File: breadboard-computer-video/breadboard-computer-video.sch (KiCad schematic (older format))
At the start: 20 parts, among them Q1 Q_NPN_BCE, Q2 Q_NPN_BCE, U1 74LS04, U2 74LS163, U3 74LS32, U4 74LS08, U5 74LS163, U6 74LS14, U7 28C256, U8 74LS02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

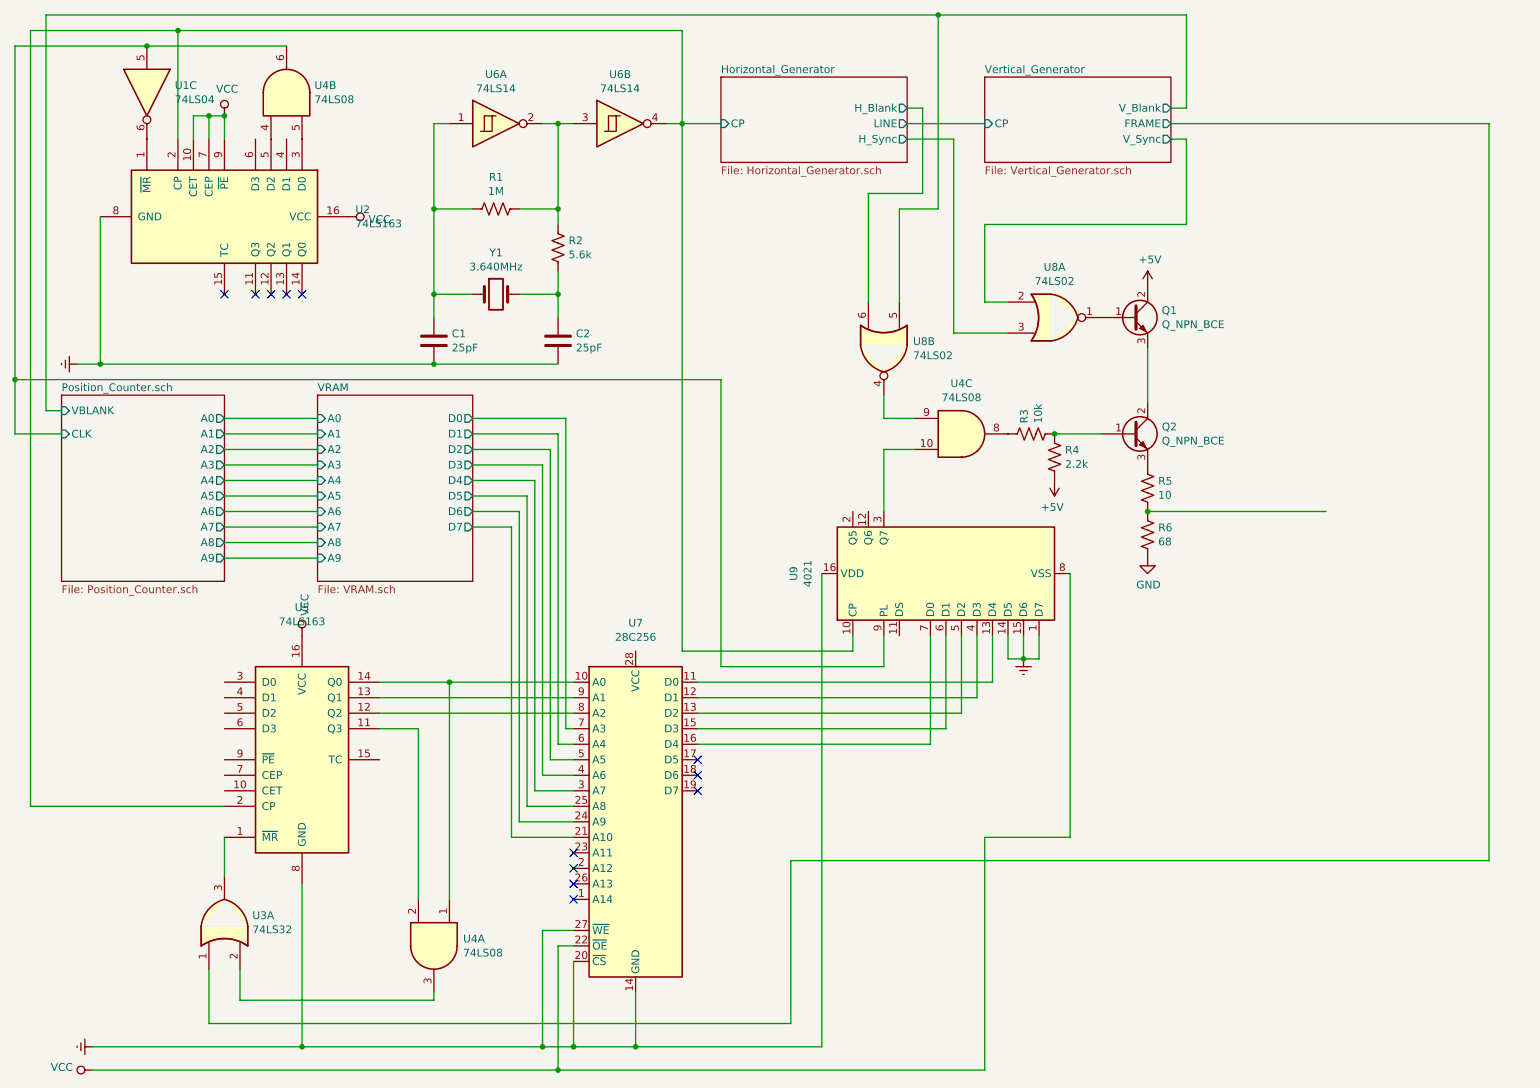
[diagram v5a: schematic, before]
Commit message: Eliminated a redundant 74ls163, which was only necessary when the character cells were not of equal width and height
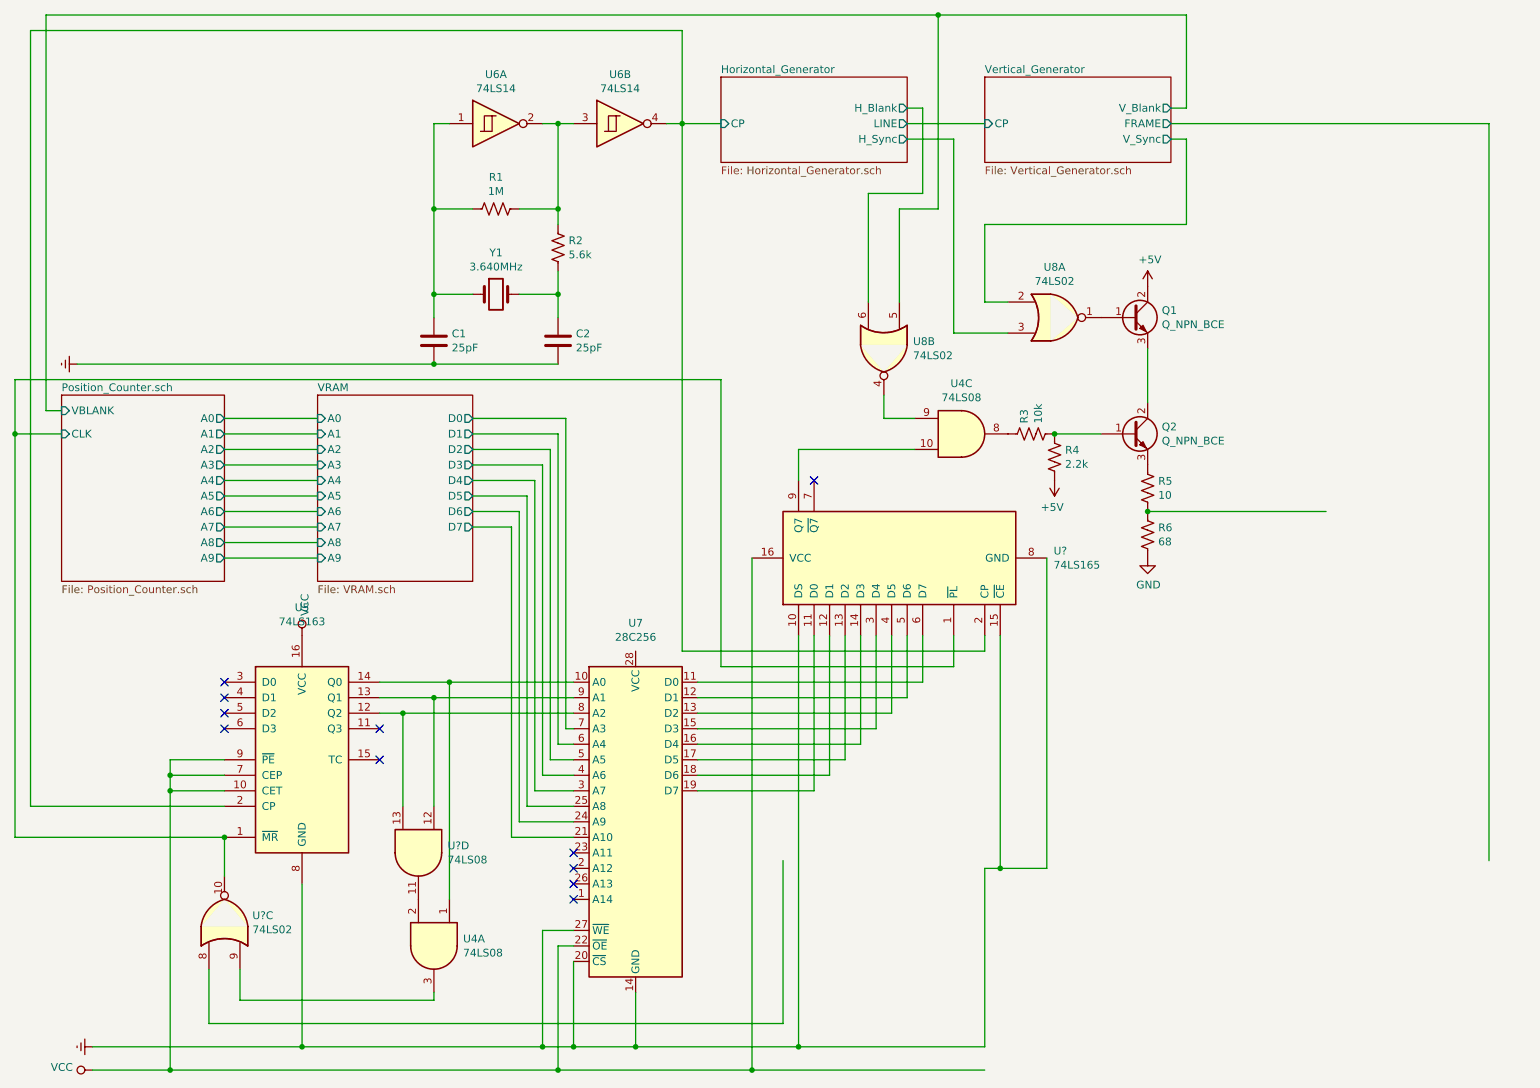
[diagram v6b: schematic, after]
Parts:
- removed U1: 74LS04, symbol 74xx:74LS04
- removed U2: 74LS163, symbol 74xx:74LS163
- removed U3: 74LS32, symbol 74xx:74LS32
- removed unit 2 of U4
- removed U9: 4021, symbol 4xxx:4021
- added U?: 74LS02, symbol 74xx:74LS02
- added U?: 74LS08, symbol 74xx:74LS08
- added U?: 74LS165, symbol 74xx:74LS165
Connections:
- net Earth: now also U?.10 (DS), U?.15 (~CE), U?.8 (GND)
- net Horizontal_Generator/CP: now also U?.2 (CP)
- net Position_Counter.sch/CLK: now also U5.1 (~MR), U?.1 (~PL), U?.10
- net VCC: now also U5.10 (CET), U5.7 (CEP), U5.9 (~PE), U?.16 (VCC)
- net at U7.11 (D0): now also U?.6 (D7)
- net at U4.10: now also U?.9 (Q7)
- net at U7.12 (D1): now also U?.5 (D6)
- net at U7.13 (D2): now also U?.4 (D5)
- net at U7.15 (D3): now also U?.3 (D4)
- net at U7.16 (D4): now also U?.14 (D3)
- net at U4.2: now also U?.11; no longer U5.11 (Q3)
- net at U4.3: now also U?.9
- net at U5.12 (Q2), U7.8 (A2): now also U?.13
- net at U5.13 (Q1), U7.9 (A1): now also U?.12
- net at U7.17 (D5): now also U?.13 (D2)
- net at U7.18 (D6): now also U?.12 (D1)
- net at U7.19 (D7): now also U?.11 (D0)
- no-connect marks 12 -> 11
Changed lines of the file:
@@
 $EndComp
-Wire Wire Line
-	5000 5200 6900 5200
-Wire Wire Line
-	5000 5300 6800 5300
-Wire Wire Line
-	5000 5400 6700 5400
-Wire Wire Line
-	5000 5500 6600 5500
 Wire Wire Line
 	4200 5200 3400 5200
@@
 $EndComp
 Wire Wire Line
-	2950 5500 3200 5500
-Wire Wire Line
-	3200 5500 3200 6600
-Wire Wire Line
 	8050 1600 10100 1600
 Wire Wire Line
 	10100 1600 10100 6350
 Wire Wire Line
-	10100 6350 5600 6350
-Wire Wire Line
-	5600 6350 5600 7400
-Wire Wire Line
-	5600 7400 1850 7400
+	5550 6350 5550 7400
+Wire Wire Line
+	5550 7400 1850 7400
 Wire Wire Line
 	1850 7400 1850 7050
@@
 Wire Wire Line
 	1950 6200 1950 6450
-$Comp
-L 74xx:74LS32 U3
-U 1 1 5DC0297B
-P 1950 6750
-F 0 "U3" V 1996 6570 50  0000 R CNN
-F 1 "74LS32" V 1905 6570 50  0000 R CNN
-F 2 "" H 1950 6750 50  0001 C CNN
-F 3 "http://www.ti.com/lit/gpn/sn74LS32" H 1950 6750 50  0001 C CNN
-	1    1950 6750
-	0    -1   -1   0
-$EndComp
 Wire Wire Line
 	2050 7050 2050 7250
@@
 Wire Wire Line
 	4900 1600 4900 1000
-Wire Wire Line
-	4900 1000 1650 1000
 Wire Wire Line
 	700  1000 700  6000
@@
 	3400 6600 3400 5400
 Wire Wire Line
-	6000 5000 4900 5000
-Wire Wire Line
 	4900 5000 4900 1600
 Wire Wire Line
-	2950 5400 4200 5400
-Wire Wire Line
-	2950 5300 3400 5300
+	2950 5400 3100 5400
+Wire Wire Line
+	2950 5300 3300 5300
 Connection ~ 3400 5200
 Wire Wire Line
@@
 $EndComp
 Wire Wire Line
-	5000 5600 6500 5600
-NoConn ~ 5000 5900
-NoConn ~ 5000 5800
-NoConn ~ 5000 5700
-Wire Wire Line
 	3550 3500 4150 3500
 Wire Wire Line
@@
 Connection ~ 2450 7550
 Wire Wire Line
-	2450 7550 1100 7550
-Wire Wire Line
-	6500 4900 6500 5600
-Wire Wire Line
-	6600 4900 6600 5500
-Wire Wire Line
-	6700 4900 6700 5400
-Wire Wire Line
-	6800 4900 6800 5300
-Wire Wire Line
-	6900 5200 6900 4900
-Wire Wire Line
-	6000 4900 6000 5000
-Wire Wire Line
-	4600 7550 5800 7550
-$Comp
-L 4xxx:4021 U9
-U 1 1 5D92BCAE
-P 6600 4500
-F 0 "U9" H 6600 5481 50  0000 C CNN
-F 1 "4021" H 6600 5390 50  0000 C CNN
-F 2 "" H 6600 4650 50  0001 C CNN
-F 3 "https://assets.nexperia.com/documents/data-sheet/HEF4021B.pdf" H 6600 4650 50  0001 C CNN
-	1    6600 4500
-	0    -1   -1   0
-$EndComp
-Wire Wire Line
-	5800 4500 5800 7550
-Wire Wire Line
 	4200 6900 4100 6900
 Wire Wire Line
@@
 	4000 7550 4200 7550
 Wire Wire Line
-	6850 7700 4100 7700
-Wire Wire Line
-	6850 7700 6850 6200
-Wire Wire Line
-	6850 6200 7400 6200
-Wire Wire Line
-	7400 6200 7400 4500
+	6850 7700 5350 7700
 Wire Wire Line
 	4100 6900 4100 7700
 Connection ~ 4100 7700
 Wire Wire Line
-	4100 7700 1100 7700
+	4100 7700 1600 7700
 $Comp
 L power:VCC #PWR?
@@
 Wire Wire Line
 	800  3450 900  3450
-$Comp
-L 74xx:74LS163 U2
-U 1 1 5E36C15A
-P 1950 2200
-F 0 "U2" V 1904 3044 50  0000 L CNN
-F 1 "74LS163" V 1995 3044 50  0000 L CNN
-F 2 "" H 1950 2200 50  0001 C CNN
-F 3 "http://www.ti.com/lit/gpn/sn74LS163" H 1950 2200 50  0001 C CNN
-	1    1950 2200
-	0    1    1    0
-$EndComp
-Wire Wire Line
-	1650 1700 1650 1000
-Connection ~ 1650 1000
-Wire Wire Line
-	1650 1000 700  1000
-$Comp
-L 74xx:74LS08 U4
-U 2 1 5E37DDE5
-P 2350 1400
-F 0 "U4" V 2396 1220 50  0000 R CNN
-F 1 "74LS08" V 2305 1220 50  0000 R CNN
-F 2 "" H 2350 1400 50  0001 C CNN
-F 3 "http://www.ti.com/lit/gpn/sn74LS08" H 2350 1400 50  0001 C CNN
-	2    2350 1400
-	0    -1   -1   0
-$EndComp
-Wire Wire Line
-	2350 1100 1450 1100
-Wire Wire Line
-	1450 1100 600  1100
 Wire Wire Line
 	600  3600 900  3600
-Connection ~ 1450 1100
-NoConn ~ 2450 2700
-NoConn ~ 2350 2700
-NoConn ~ 2250 2700
-NoConn ~ 2150 2700
-NoConn ~ 1950 2700
-$Comp
-L 74xx:74LS04 U1
-U 3 1 5E3AF993
-P 1450 1400
-F 0 "U1" V 1404 1580 50  0000 L CNN
-F 1 "74LS04" V 1495 1580 50  0000 L CNN
-F 2 "" H 1450 1400 50  0001 C CNN
-F 3 "http://www.ti.com/lit/gpn/sn74LS04" H 1450 1400 50  0001 C CNN
-	3    1450 1400
-	0    1    1    0
-$EndComp
-$Comp
-L power:VCC #PWR?
-U 1 1 5E3BFB68
-P 1950 1550
-F 0 "#PWR?" H 1950 1400 50  0001 C CNN
-F 1 "VCC" H 1967 1723 50  0000 C CNN
-F 2 "" H 1950 1550 50  0001 C CNN
-F 3 "" H 1950 1550 50  0001 C CNN
-	1    1950 1550
-	1    0    0    -1
-$EndComp
-Wire Wire Line
-	1950 1550 1850 1550
-Wire Wire Line
-	1750 1550 1750 1700
-Wire Wire Line
-	1850 1700 1850 1550
-Connection ~ 1850 1550
-Wire Wire Line
-	1850 1550 1750 1550
-Wire Wire Line
-	1950 1550 1950 1700
-Connection ~ 1950 1550
-$Comp
-L power:Earth #PWR?
-U 1 1 5E3D9597
-P 7100 5050
-F 0 "#PWR?" H 7100 4800 50  0001 C CNN
-F 1 "Earth" H 7100 4900 50  0001 C CNN
-F 2 "" H 7100 5050 50  0001 C CNN
-F 3 "~" H 7100 5050 50  0001 C CNN
-	1    7100 5050
-	1    0    0    -1
-$EndComp
-Wire Wire Line
-	7100 5050 7100 4900
-Wire Wire Line
-	7000 4900 7000 5050
-Wire Wire Line
-	7000 5050 7100 5050
-Connection ~ 7100 5050
-Wire Wire Line
-	7100 5050 7200 5050
-Wire Wire Line
-	7200 5050 7200 4900
-Wire Wire Line
-	6200 4900 6200 5100
-Wire Wire Line
-	6200 5100 5150 5100
+Wire Wire Line
+	6650 5100 5150 5100
 Wire Wire Line
 	3550 4200 3800 4200
@@
 	5150 3250 5150 5100
 Wire Wire Line
-	600  1100 600  3250
-Wire Wire Line
 	600  3250 600  3600
-Connection ~ 600  3250
 Wire Wire Line
 	1950 3500 2550 3500
@@
 	4100 3150 3300 3150
 Connection ~ 3300 3150
-Wire Wire Line
-	3300 3150 1150 3150
-Connection ~ 1150 3150
-Wire Wire Line
-	1150 3150 1000 3150
-Wire Wire Line
-	1150 2200 1150 3150
 $Comp
 L power:Earth #PWR?
@@
 $EndComp
 $Comp
-L power:VCC #PWR?
-U 1 1 5E98E66C
-P 2750 2200
-F 0 "#PWR?" H 2750 2050 50  0001 C CNN
-F 1 "VCC" V 2767 2328 50  0000 L CNN
-F 2 "" H 2750 2200 50  0001 C CNN
-F 3 "" H 2750 2200 50  0001 C CNN
-	1    2750 2200
-	0    1    1    0
-$EndComp
-$Comp
 L 74xx:74LS08 U4
 U 3 1 5E99B421
@@
 $EndComp
 Wire Wire Line
-	6400 3700 6200 3700
-Wire Wire Line
-	6200 3700 6200 4100
-Wire Wire Line
 	6200 3350 6200 3500
 Wire Wire Line
@@
 	1    0    0    -1
 $EndComp
+$Comp
+L 74xx:74LS02 U?
+U 3 1 5DC8E486
+P 1950 6750
+F 0 "U?" V 1996 6570 50  0000 R CNN
+F 1 "74LS02" V 1905 6570 50  0000 R CNN
+F 2 "" H 1950 6750 50  0001 C CNN
+F 3 "http://www.ti.com/lit/gpn/sn74ls02" H 1950 6750 50  0001 C CNN
+	3    1950 6750
+	0    -1   -1   0
+$EndComp
+NoConn ~ 1950 5500
+NoConn ~ 1950 5400
+NoConn ~ 1950 5300
+NoConn ~ 1950 5200
+Wire Wire Line
+	1950 5700 1600 5700
+Wire Wire Line
+	1600 5700 1600 5800
+Connection ~ 1600 7700
+Wire Wire Line
+	1600 7700 1100 7700
+NoConn ~ 2950 5700
+$Comp
+L 74xx:74LS08 U?
+U 4 1 5DCE6604
+P 3200 6300
+F 0 "U?" V 3154 6488 50  0000 L CNN
+F 1 "74LS08" V 3245 6488 50  0000 L CNN
+F 2 "" H 3200 6300 50  0001 C CNN
+F 3 "http://www.ti.com/lit/gpn/sn74LS08" H 3200 6300 50  0001 C CNN
+	4    3200 6300
+	0    1    1    0
+$EndComp
+Wire Wire Line
+	3100 6000 3100 5400
+Connection ~ 3100 5400
+Wire Wire Line
+	3100 5400 4200 5400
+Wire Wire Line
+	3300 6000 3300 5300
+Connection ~ 3300 5300
+Wire Wire Line
+	3300 5300 3400 5300
+Wire Wire Line
+	5000 5400 6250 5400
+Wire Wire Line
+	5000 5500 6150 5500
+Wire Wire Line
+	5000 5600 6050 5600
+Wire Wire Line
+	5000 5700 5950 5700
+Wire Wire Line
+	5000 5800 5850 5800
+Wire Wire Line
+	5000 5900 5750 5900
+$Comp
+L 74xx:74LS165 U?
+U 1 1 5DD7AB27
+P 6250 4400
+F 0 "U?" V 6296 3356 50  0000 R CNN
+F 1 "74LS165" V 6205 3356 50  0000 R CNN
+F 2 "" H 6250 4400 50  0001 C CNN
+F 3 "http://www.ti.com/lit/gpn/sn74LS165" H 6250 4400 50  0001 C CNN
+	1    6250 4400
+	0    -1   -1   0
+$EndComp
+Wire Wire Line
+	5000 5200 6450 5200
+Wire Wire Line
+	5000 5300 6350 5300
+Wire Wire Line
+	6650 4900 6650 5100
+Wire Wire Line
+	5750 5900 5750 4900
+Wire Wire Line
+	5850 5800 5850 4900
+Wire Wire Line
+	5950 5700 5950 4900
+Wire Wire Line
+	6350 4900 6350 5300
+Wire Wire Line
+	6250 4900 6250 5400
+Wire Wire Line
+	6850 4900 6850 5000
+Wire Wire Line
+	6450 5200 6450 4900
+Wire Wire Line
+	6050 4900 6050 5600
+Wire Wire Line
+	6150 4900 6150 5500
+Wire Wire Line
+	6850 5000 4900 5000
+Wire Wire Line
+	5650 3700 5650 3900
+Wire Wire Line
+	5650 3700 6400 3700
+Wire Wire Line
+	6850 7550 6850 6400
+Wire Wire Line
+	4600 7550 5650 7550
+Wire Wire Line
+	5350 7700 5350 4400
+Connection ~ 5350 7700
+Wire Wire Line
+	5350 7700 4100 7700
+Wire Wire Line
+	7250 4400 7250 6400
+Wire Wire Line
+	6850 6400 6950 6400
+Wire Wire Line
+	5650 4900 5650 7550
+Connection ~ 5650 7550
+Wire Wire Line
+	5650 7550 6850 7550
+Wire Wire Line
+	6950 4900 6950 6400
+Connection ~ 6950 6400
+Wire Wire Line
+	6950 6400 7250 6400
+NoConn ~ 5750 3900
+Wire Wire Line
+	1100 7550 2450 7550
+Wire Wire Line
+	1600 5800 1950 5800
+Connection ~ 1600 5800
+Wire Wire Line
+	1600 5800 1600 5900
+Wire Wire Line
+	1600 5900 1950 5900
+Connection ~ 1600 5900
+Wire Wire Line
+	1600 5900 1600 7700
+Wire Wire Line
+	700  1000 4900 1000
+Wire Wire Line
+	1000 3150 3300 3150
+Wire Wire Line
+	600  3600 600  6200
+Wire Wire Line
+	600  6200 1950 6200
+Connection ~ 600  3600
+Connection ~ 1950 6200
+NoConn ~ 2950 5500
 $EndSCHEMATC

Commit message: various things
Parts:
- Y1: value 3.640MHz -> 12MHz
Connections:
- net Vertical_Generator/FRAME: now also U?.8
- net CVBS_Output: now reaches R5.2, R6.1
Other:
- moved on the sheet: C1, C2, R1, R2, U6A, U6B, Y1
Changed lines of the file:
@@
 L Device:C C1
 U 1 1 5D9AD126
-P 3300 3000
-F 0 "C1" H 3415 3046 50  0000 L CNN
-F 1 "25pF" H 3415 2955 50  0000 L CNN
-F 2 "" H 3338 2850 50  0001 C CNN
-F 3 "~" H 3300 3000 50  0001 C CNN
-	1    3300 3000
+P 3200 3000
+F 0 "C1" H 3315 3046 50  0000 L CNN
+F 1 "25pF" H 3315 2955 50  0000 L CNN
+F 2 "" H 3238 2850 50  0001 C CNN
+F 3 "~" H 3200 3000 50  0001 C CNN
+	1    3200 3000
 	1    0    0    -1
 $EndComp
@@
 L Device:C C2
 U 1 1 5D9ADB4B
-P 4100 3000
-F 0 "C2" H 4215 3046 50  0000 L CNN
-F 1 "25pF" H 4215 2955 50  0000 L CNN
-F 2 "" H 4138 2850 50  0001 C CNN
-F 3 "~" H 4100 3000 50  0001 C CNN
-	1    4100 3000
+P 4000 3000
+F 0 "C2" H 4115 3046 50  0000 L CNN
+F 1 "25pF" H 4115 2955 50  0000 L CNN
+F 2 "" H 4038 2850 50  0001 C CNN
+F 3 "~" H 4000 3000 50  0001 C CNN
+	1    4000 3000
 	1    0    0    -1
 $EndComp
@@
 L Device:Crystal Y1
 U 1 1 5D9AE745
-P 3700 2700
-F 0 "Y1" H 3700 2968 50  0000 C CNN
-F 1 "3.640MHz" H 3700 2877 50  0000 C CNN
-F 2 "" H 3700 2700 50  0001 C CNN
-F 3 "https://www.mouser.com/datasheet/2/741/LFXTAL036736Bulk-998720.pdf" H 3700 2700 50  0001 C CNN
-	1    3700 2700
+P 3600 2700
+F 0 "Y1" H 3600 2968 50  0000 C CNN
+F 1 "12MHz" H 3600 2877 50  0000 C CNN
+F 2 "" H 3600 2700 50  0001 C CNN
+F 3 "https://www.mouser.com/datasheet/2/741/LFXTAL036736Bulk-998720.pdf" H 3600 2700 50  0001 C CNN
+	1    3600 2700
 	1    0    0    -1
 $EndComp
@@
 L Device:R_US R2
 U 1 1 5D9AF295
-P 4100 2400
-F 0 "R2" H 4168 2446 50  0000 L CNN
-F 1 "5.6k" H 4168 2355 50  0000 L CNN
-F 2 "" V 4140 2390 50  0001 C CNN
-F 3 "~" H 4100 2400 50  0001 C CNN
-	1    4100 2400
+P 4000 2400
+F 0 "R2" H 4068 2446 50  0000 L CNN
+F 1 "5.6k" H 4068 2355 50  0000 L CNN
+F 2 "" V 4040 2390 50  0001 C CNN
+F 3 "~" H 4000 2400 50  0001 C CNN
+	1    4000 2400
 	1    0    0    -1
 $EndComp
@@
 L Device:R_US R1
 U 1 1 5D9AFC84
-P 3700 2150
-F 0 "R1" V 3495 2150 50  0000 C CNN
-F 1 "1M" V 3586 2150 50  0000 C CNN
-F 2 "" V 3740 2140 50  0001 C CNN
-F 3 "~" H 3700 2150 50  0001 C CNN
-	1    3700 2150
+P 3600 2150
+F 0 "R1" V 3395 2150 50  0000 C CNN
+F 1 "1M" V 3486 2150 50  0000 C CNN
+F 2 "" V 3640 2140 50  0001 C CNN
+F 3 "~" H 3600 2150 50  0001 C CNN
+	1    3600 2150
 	0    1    1    0
 $EndComp
 Wire Wire Line
-	3300 2850 3300 2700
-Wire Wire Line
-	3300 1600 3400 1600
-Wire Wire Line
-	4000 1600 4100 1600
-Wire Wire Line
-	4100 1600 4100 2150
-Wire Wire Line
-	4100 2550 4100 2700
-Wire Wire Line
-	3850 2700 4100 2700
-Connection ~ 4100 2700
-Wire Wire Line
-	4100 2700 4100 2850
-Wire Wire Line
-	3550 2700 3300 2700
-Connection ~ 3300 2700
-Wire Wire Line
-	3300 2700 3300 2150
-Wire Wire Line
-	3550 2150 3300 2150
-Connection ~ 3300 2150
-Wire Wire Line
-	3300 2150 3300 1600
-Wire Wire Line
-	3850 2150 4100 2150
-Connection ~ 4100 2150
-Wire Wire Line
-	4100 2150 4100 2250
-Wire Wire Line
-	4200 1600 4100 1600
-Connection ~ 4100 1600
+	3200 2850 3200 2700
+Wire Wire Line
+	3200 1600 3300 1600
+Wire Wire Line
+	3900 1600 4000 1600
+Wire Wire Line
+	4000 1600 4000 2150
+Wire Wire Line
+	4000 2550 4000 2700
+Wire Wire Line
+	3750 2700 4000 2700
+Connection ~ 4000 2700
+Wire Wire Line
+	4000 2700 4000 2850
+Wire Wire Line
+	3450 2700 3200 2700
+Connection ~ 3200 2700
+Wire Wire Line
+	3200 2700 3200 2150
+Wire Wire Line
+	3450 2150 3200 2150
+Connection ~ 3200 2150
+Wire Wire Line
+	3200 2150 3200 1600
+Wire Wire Line
+	3750 2150 4000 2150
+Connection ~ 4000 2150
+Wire Wire Line
+	4000 2150 4000 2250
+Wire Wire Line
+	4100 1600 4000 1600
+Connection ~ 4000 1600
 Wire Wire Line
 	7600 3600 7300 3600
@@
 	8050 1600 10100 1600
 Wire Wire Line
-	10100 1600 10100 6350
-Wire Wire Line
-	5550 6350 5550 7400
+	10100 1600 10100 6300
 Wire Wire Line
 	5550 7400 1850 7400
@@
 	700  6000 1950 6000
 Connection ~ 4900 1600
-Wire Wire Line
-	4900 1600 4800 1600
 Wire Wire Line
 	3400 6600 3400 5400
@@
 F19 "D7" O R 3550 4200 50
 $EndSheet
-Wire Wire Line
-	4100 3150 3300 3150
-Connection ~ 3300 3150
 $Comp
 L power:Earth #PWR?
 U 1 1 5E98DD67
-P 1000 3150
-F 0 "#PWR?" H 1000 2900 50  0001 C CNN
-F 1 "Earth" H 1000 3000 50  0001 C CNN
-F 2 "" H 1000 3150 50  0001 C CNN
-F 3 "~" H 1000 3150 50  0001 C CNN
-	1    1000 3150
+P 2900 3150
+F 0 "#PWR?" H 2900 2900 50  0001 C CNN
+F 1 "Earth" H 2900 3000 50  0001 C CNN
+F 2 "" H 2900 3150 50  0001 C CNN
+F 3 "~" H 2900 3150 50  0001 C CNN
+	1    2900 3150
 	0    1    1    0
 $EndComp
@@
 L 74xx:74LS14 U6
 U 1 1 5EA1FAA0
-P 3700 1600
-F 0 "U6" H 3700 1917 50  0000 C CNN
-F 1 "74LS14" H 3700 1826 50  0000 C CNN
-F 2 "" H 3700 1600 50  0001 C CNN
-F 3 "http://www.ti.com/lit/gpn/sn74LS14" H 3700 1600 50  0001 C CNN
-	1    3700 1600
+P 3600 1600
+F 0 "U6" H 3600 1917 50  0000 C CNN
+F 1 "74LS14" H 3600 1826 50  0000 C CNN
+F 2 "" H 3600 1600 50  0001 C CNN
+F 3 "http://www.ti.com/lit/gpn/sn74LS14" H 3600 1600 50  0001 C CNN
+	1    3600 1600
 	1    0    0    -1
 $EndComp
@@
 L 74xx:74LS14 U6
 U 2 1 5EA2147E
-P 4500 1600
-F 0 "U6" H 4500 1917 50  0000 C CNN
-F 1 "74LS14" H 4500 1826 50  0000 C CNN
-F 2 "" H 4500 1600 50  0001 C CNN
-F 3 "http://www.ti.com/lit/gpn/sn74LS14" H 4500 1600 50  0001 C CNN
-	2    4500 1600
+P 4400 1600
+F 0 "U6" H 4400 1917 50  0000 C CNN
+F 1 "74LS14" H 4400 1826 50  0000 C CNN
+F 2 "" H 4400 1600 50  0001 C CNN
+F 3 "http://www.ti.com/lit/gpn/sn74LS14" H 4400 1600 50  0001 C CNN
+	2    4400 1600
 	1    0    0    -1
 $EndComp
@@
 	700  1000 4900 1000
 Wire Wire Line
-	1000 3150 3300 3150
+	2900 3150 3200 3150
 Wire Wire Line
 	600  3600 600  6200
@@
 Connection ~ 1950 6200
 NoConn ~ 2950 5500
+Connection ~ 3200 3150
+Wire Wire Line
+	3200 3150 4000 3150
+Wire Wire Line
+	5550 6300 10100 6300
+Wire Wire Line
+	5550 6300 5550 7400
+Text HLabel 9050 4100 2    50   Output ~ 0
+CVBS_Output
+Wire Wire Line
+	4700 1600 4900 1600
 $EndSCHEMATC
